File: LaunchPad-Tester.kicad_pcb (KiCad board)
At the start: 2 copper layers, 50.8 x 30.5 mm, 10 parts, among them U1 CY8C9540A

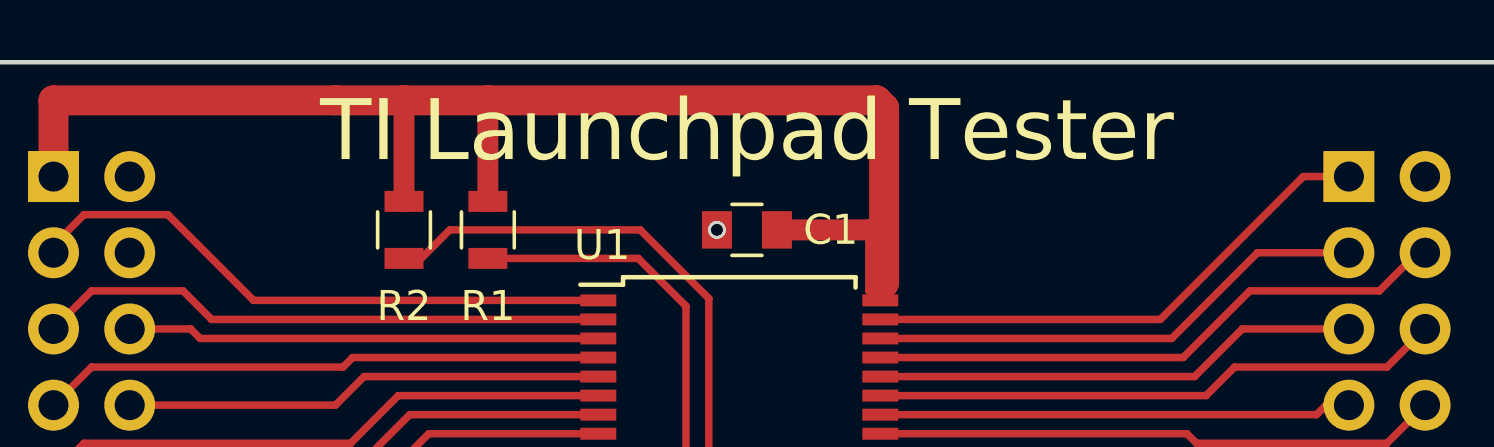
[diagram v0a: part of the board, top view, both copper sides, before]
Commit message: Renamed project to LaunchPad-Tester and coorected some typos.
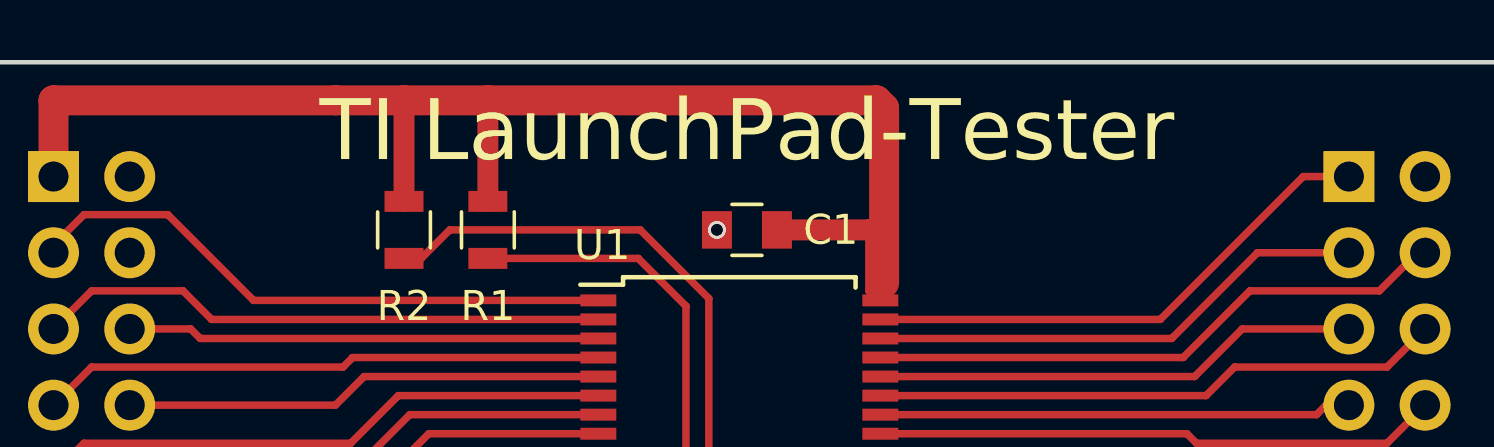
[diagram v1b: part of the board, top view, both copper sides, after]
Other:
- board text added: "TI LaunchPad-Tester"
- board text removed: "TI Launchpad Tester"
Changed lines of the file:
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@@
-(kicad_pcb (version 4) (host pcbnew 4.0.6-e0-6349~53~ubuntu16.04.1)
+(kicad_pcb (version 4) (host pcbnew 4.0.7-e2-6376~58~ubuntu16.04.1)
   (general
     (links 53)
@@
     )
   )
-  (gr_text "TI Launchpad Tester" (at 150.114 89.916) (layer F.SilkS)
+  (gr_text "TI LaunchPad-Tester" (at 150.114 89.916) (layer F.SilkS)
     (effects (font (size 2.032 2.032) (thickness 0.381)))
   )
